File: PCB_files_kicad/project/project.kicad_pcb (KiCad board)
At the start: 2 copper layers, 65 x 100 mm, 51 parts, among them J1 Conn_01x08_Female, J2 S1, J3 S2, J4 Conn_01x08_Female, J5 Display, J6 HC06, J7 Barrel_Jack, J8 USB_B_Micro, Q1 IRF9Z20, U1 M24C02, U2 TP4056, U3 MT3608, U4 BluePill_Connector

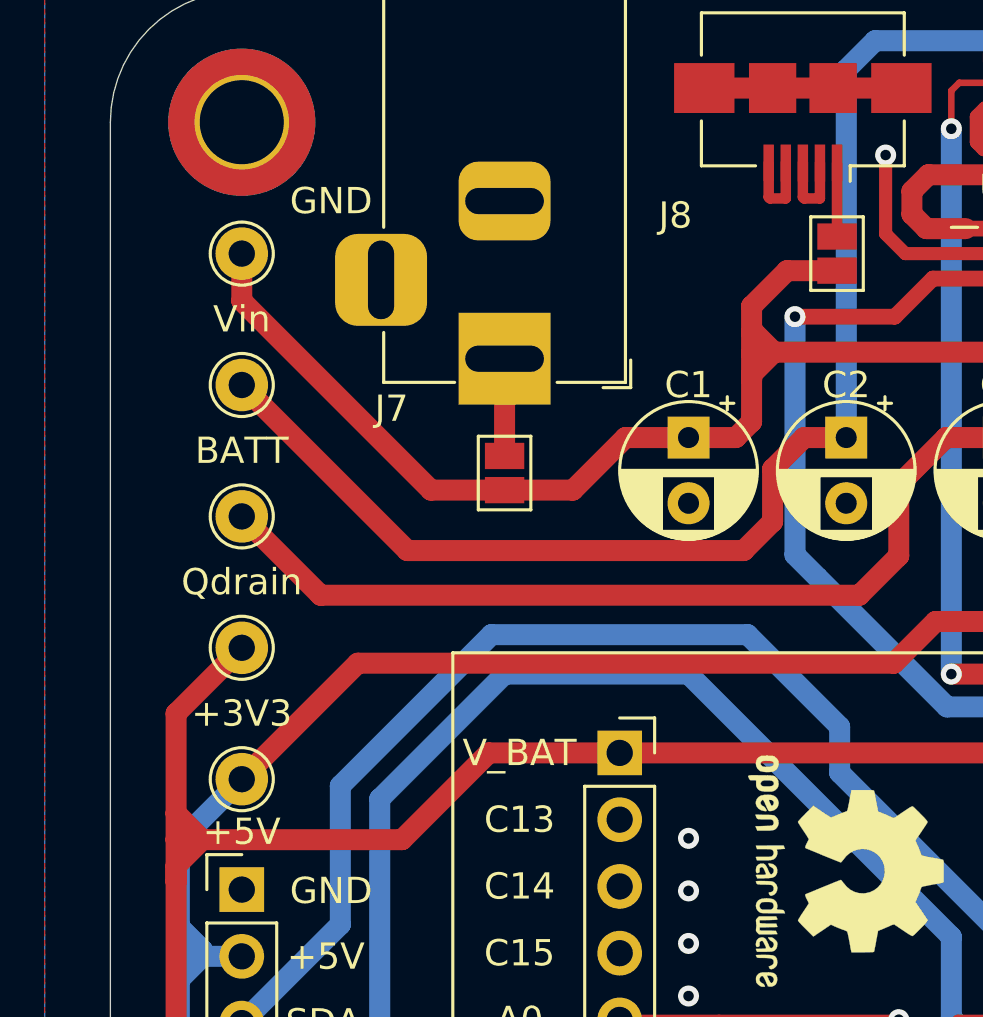
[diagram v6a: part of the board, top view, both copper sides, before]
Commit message: Schematic v1.6
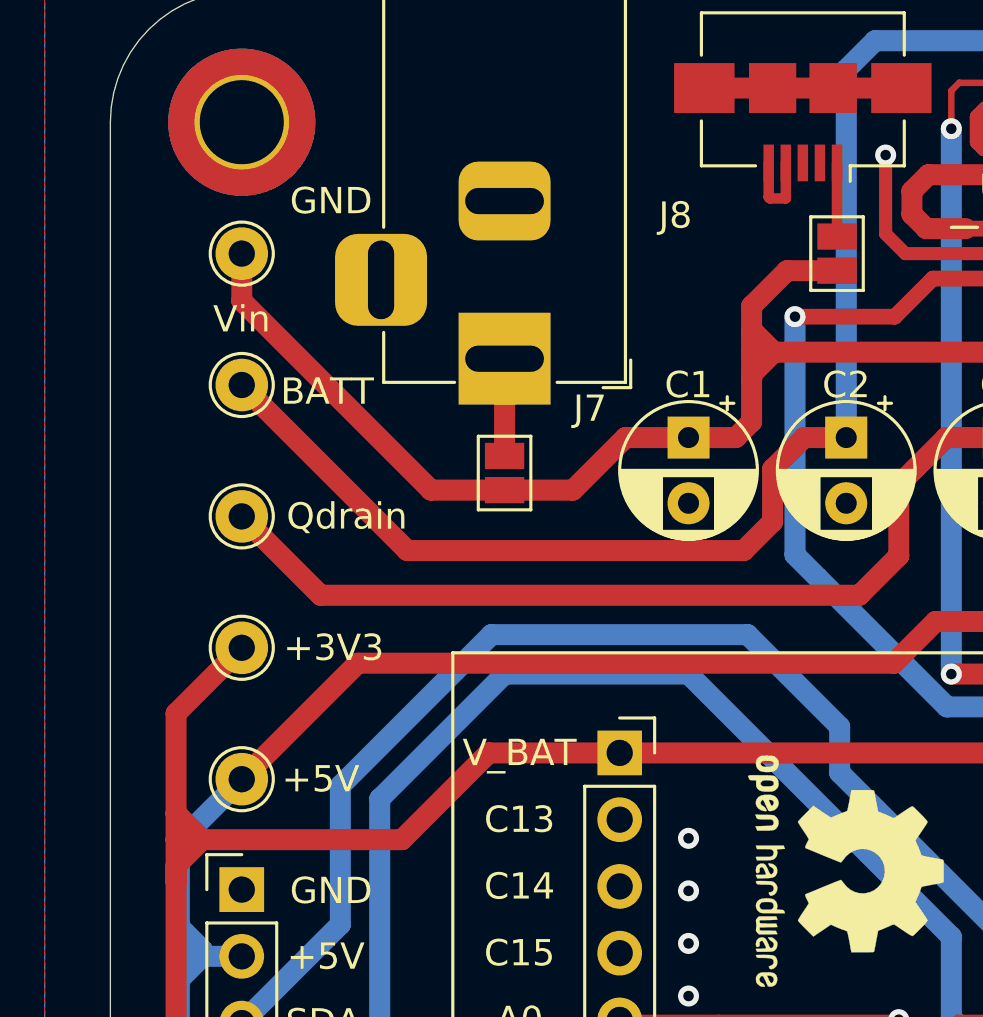
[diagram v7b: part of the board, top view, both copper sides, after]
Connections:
- J8 pad 3: Net-(J8-Pad2) -> Net-(J8-Pad3)
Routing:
- net Net-(J8-Pad2): track 3.32 -> 0.00 mm
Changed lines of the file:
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@@
     (thickness 1.6)
     (drawings 37)
-    (tracks 532)
+    (tracks 528)
     (zones 0)
     (modules 51)
-    (nets 54)
+    (nets 55)
   )
   (page A4)
@@
   )
   (setup
-    (last_trace_width 0.8)
+    (last_trace_width 0.25)
     (user_trace_width 0.4)
     (user_trace_width 0.5)
@@
   (net 52 "Net-(U4-Pad3)")
   (net 53 "Net-(U2-Pad7)")
+  (net 54 "Net-(J8-Pad3)")
   (net_class Default "This is the default net class."
     (clearance 0.2)
@@
     (add_net "Net-(J8-Pad1)")
     (add_net "Net-(J8-Pad2)")
+    (add_net "Net-(J8-Pad3)")
     (add_net "Net-(R10-Pad2)")
     (add_net "Net-(R3-Pad2)")
@@
     (tags "test point THT pad")
     (attr virtual)
-    (fp_text reference +3V3 (at 0 2.5) (layer F.SilkS)
+    (fp_text reference +3V3 (at 3.5 0) (layer F.SilkS)
       (effects (font (size 1 1) (thickness 0.15)))
     )
@@
       (effects (font (size 1 1) (thickness 0.15)))
     )
+    (fp_circle (center 0 0) (end 1.5 0) (layer F.CrtYd) (width 0.05))
+    (fp_circle (center 0 0) (end 0 1.2) (layer F.SilkS) (width 0.12))
     (fp_text user %R (at 0 -2) (layer F.Fab)
       (effects (font (size 1 1) (thickness 0.15)))
     )
-    (fp_circle (center 0 0) (end 1.5 0) (layer F.CrtYd) (width 0.05))
-    (fp_circle (center 0 0) (end 0 1.2) (layer F.SilkS) (width 0.12))
     (pad 1 thru_hole circle (at 0 0) (size 2 2) (drill 1) (layers *.Cu *.Mask)
       (net 23 +3V3))
@@
       (effects (font (size 1 1) (thickness 0.15)))
     )
-    (fp_arc (start -2.6 -0.5) (end -2.6 -1.2) (angle -90) (layer F.SilkS) (width 0.12))
-    (fp_arc (start -2.6 0.5) (end -3.3 0.5) (angle -90) (layer F.SilkS) (width 0.12))
-    (fp_arc (start 2.6 0.5) (end 2.6 1.2) (angle -90) (layer F.SilkS) (width 0.12))
-    (fp_arc (start 2.6 -0.5) (end 3.3 -0.5) (angle -90) (layer F.SilkS) (width 0.12))
     (fp_line (start 3.5 1.25) (end -3.5 1.25) (layer F.CrtYd) (width 0.05))
     (fp_line (start 3.5 1.25) (end 3.5 -1.25) (layer F.CrtYd) (width 0.05))
@@
     (fp_line (start -1.95 1.5) (end -1.95 3.5) (layer F.SilkS) (width 0.12))
     (fp_line (start -2.95 2.5) (end -0.95 2.5) (layer F.SilkS) (width 0.12))
+    (fp_arc (start -2.6 -0.5) (end -2.6 -1.2) (angle -90) (layer F.SilkS) (width 0.12))
+    (fp_arc (start -2.6 0.5) (end -3.3 0.5) (angle -90) (layer F.SilkS) (width 0.12))
+    (fp_arc (start 2.6 0.5) (end 2.6 1.2) (angle -90) (layer F.SilkS) (width 0.12))
+    (fp_arc (start 2.6 -0.5) (end 3.3 -0.5) (angle -90) (layer F.SilkS) (width 0.12))
     (pad 2 smd roundrect (at 2 0 180) (size 2 2) (layers F.Cu F.Mask) (roundrect_rratio 0.25)
       (net 1 Earth) (zone_connect 2))
@@
       (net 36 "Net-(J8-Pad2)") (zone_connect 1))
     (pad 3 smd rect (at 0 -1.55 180) (size 0.4 1.4) (layers F.Cu F.Paste F.Mask)
-      (net 36 "Net-(J8-Pad2)") (zone_connect 1))
+      (net 54 "Net-(J8-Pad3)") (zone_connect 1))
     (pad 4 smd rect (at 0.65 -1.55 180) (size 0.4 1.4) (layers F.Cu F.Paste F.Mask)
       (net 1 Earth) (zone_connect 0))
@@
     (tags "test point THT pad")
     (attr virtual)
-    (fp_text reference +5V (at 2 0 180) (layer F.SilkS)
+    (fp_text reference +5V (at 0 -3 180) (layer F.SilkS)
       (effects (font (size 1 1) (thickness 0.15)))
     )
@@
     (tags "test point THT pad")
     (attr virtual)
-    (fp_text reference Qdrain (at 2.5 0 180) (layer F.SilkS)
+    (fp_text reference Qdrain (at 0 -4 180) (layer F.SilkS)
       (effects (font (size 1 1) (thickness 0.15)))
     )
@@
     (tags "test point THT pad")
     (attr virtual)
-    (fp_text reference BATT (at 2.5 0 180) (layer F.SilkS)
+    (fp_text reference BATT (at 0.25 -3.25 180) (layer F.SilkS)
       (effects (font (size 1 1) (thickness 0.15)))
     )
@@
     (descr "DC Barrel Jack")
     (tags "Power Jack")
-    (fp_text reference J7 (at 1.9 4.3 180) (layer F.SilkS)
+    (fp_text reference J7 (at 1.9 -3.25 180) (layer F.SilkS)
       (effects (font (size 1 1) (thickness 0.15)))
     )
@@
   (segment (start 110 67.7) (end 110 64) (width 0.8) (layer F.Cu) (net 34))
   (segment (start 122.65 56.55) (end 122.65 59.35) (width 0.4) (layer F.Cu) (net 35))
-  (segment (start 122 57.9) (end 122 56.55) (width 0.4) (layer F.Cu) (net 36))
-  (segment (start 121.35 56.55) (end 121.35 57.85) (width 0.4) (layer F.Cu) (net 36))
-  (segment (start 121.4 57.9) (end 121.35 57.85) (width 0.4) (layer F.Cu) (net 36))
-  (segment (start 122 57.9) (end 121.4 57.9) (width 0.4) (layer F.Cu) (net 36))
   (segment (start 142.55 79.5) (end 138.5 79.5) (width 0.8) (layer F.Cu) (net 37))
   (via (at 127 76) (size 0.8) (drill 0.4) (layers F.Cu B.Cu) (net 37))

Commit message: Schematic v1.7 - PCB v1.4
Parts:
- added C2: 10uF, Capacitor_SMD:C_0805_2012Metric_Pad1.18x1.45mm_HandSolder, F.Cu at (120.5, 87.2)
- added U3: LM1117-3.3, Package_TO_SOT_SMD:SOT-223-3_TabPin2, F.Cu at (121.5, 80.8)
- TP1: renamed from +3V3; value TestPoint -> +3.3V
- TP2: renamed from Vin; value PowerSupply -> Vin
- TP5: renamed from +5V; value out5v -> +5V
- moved REF** 15.3 mm to (123.8, 98.8)
- turned TP2 to 0 degrees
- renumbered C2 to C3, C3 to C4, D5 to D4, D4 to D5, R4 to R10, R10 to R11, R11 to R12, R7 to R13, R12 to R2, R5 to R3, R6 to R4, R13 to R5, R2 to R6, R8 to R7, R9 to R8, R3 to R9, BATT to TP3, Qdrain to TP4, U3 to U4, U4 to U5
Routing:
- net +3V3: track 213.8 -> 224.6 mm
- net +5V: track 214.2 -> 222.6 mm
- net Earth: vias 39 -> 42
